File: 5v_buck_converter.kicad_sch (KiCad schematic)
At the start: 7 parts, among them U2 TPS562231DRLR

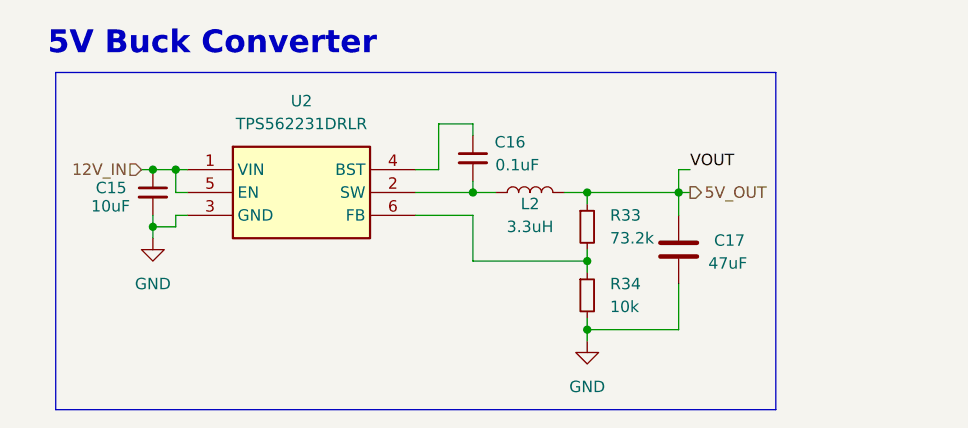
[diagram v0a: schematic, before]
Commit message: address review changes, add more output protections
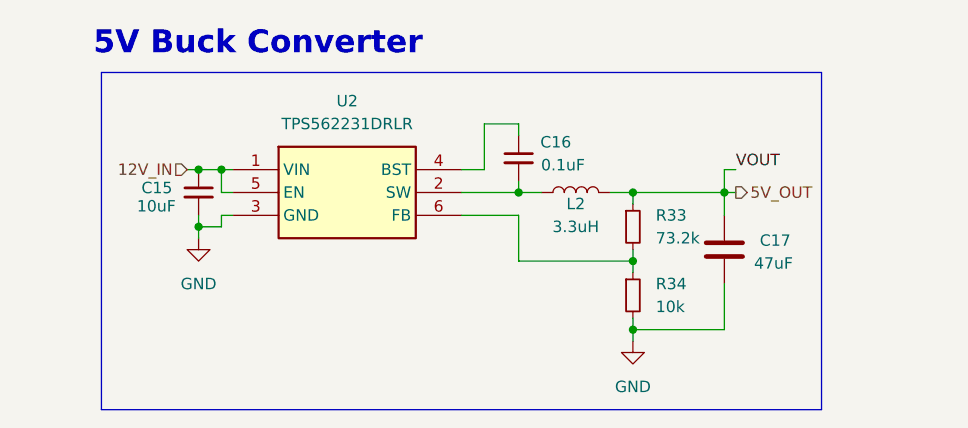
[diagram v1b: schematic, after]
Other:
- moved on the sheet: C15, C16, C17, L2, R33, R34, U2

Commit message: footprint assignment again
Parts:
- renumbered C15 to C17, C16 to C18, C17 to C19, R33 to R31, R34 to R32, U2 to U4
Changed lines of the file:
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@@
 		(on_board yes)
 		(dnp no)
-		(property "Reference" "C15"
+		(property "Reference" "C17"
 			(at 116.84 97.282 0)
 			(effects
@@
 			(project ""
 				(path "/f58400c5-df4b-4929-8d2b-33c0fe23fcd9/4f21da9f-d1d7-4b66-a00f-51f47ae1c74b"
-					(reference "C15")
+					(reference "C17")
 					(unit 1)
 				)
@@
 		(on_board yes)
 		(dnp no)
-		(property "Reference" "C17"
+		(property "Reference" "C19"
 			(at 188.976 103.124 0)
 			(effects
@@
 			(project "USBCPowerPCB"
 				(path "/f58400c5-df4b-4929-8d2b-33c0fe23fcd9/4f21da9f-d1d7-4b66-a00f-51f47ae1c74b"
-					(reference "C17")
+					(reference "C19")
 					(unit 1)
 				)
@@
 		(on_board yes)
 		(dnp no)
-		(property "Reference" "C16"
+		(property "Reference" "C18"
 			(at 164.592 92.202 0)
 			(effects
@@
 			(project "USBCPowerPCB"
 				(path "/f58400c5-df4b-4929-8d2b-33c0fe23fcd9/4f21da9f-d1d7-4b66-a00f-51f47ae1c74b"
-					(reference "C16")
+					(reference "C18")
 					(unit 1)
 				)
@@
 		(dnp no)
 		(fields_autoplaced yes)
-		(property "Reference" "R33"
+		(property "Reference" "R31"
 			(at 173.99 100.3299 0)
 			(effects
@@
 			(project "USBCPowerPCB"
 				(path "/f58400c5-df4b-4929-8d2b-33c0fe23fcd9/4f21da9f-d1d7-4b66-a00f-51f47ae1c74b"
-					(reference "R33")
+					(reference "R31")
 					(unit 1)
 				)
@@
 		(dnp no)
 		(fields_autoplaced yes)
-		(property "Reference" "R34"
+		(property "Reference" "R32"
 			(at 173.99 107.9499 0)
 			(effects
@@
 			(project ""
 				(path "/f58400c5-df4b-4929-8d2b-33c0fe23fcd9/4f21da9f-d1d7-4b66-a00f-51f47ae1c74b"
-					(reference "R34")
+					(reference "R32")
 					(unit 1)
 				)
@@
 		(dnp no)
 		(fields_autoplaced yes)
-		(property "Reference" "U2"
+		(property "Reference" "U4"
 			(at 139.7 87.63 0)
 			(effects
@@
 			(project ""
 				(path "/f58400c5-df4b-4929-8d2b-33c0fe23fcd9/4f21da9f-d1d7-4b66-a00f-51f47ae1c74b"
-					(reference "U2")
+					(reference "U4")
 					(unit 1)
 				)
@@
 		(dnp no)
 		(fields_autoplaced yes)
-		(property "Reference" "#PWR038"
+		(property "Reference" "#PWR059"
 			(at 171.45 120.65 0)
 			(effects
@@
 			(project "USBCPowerPCB"
 				(path "/f58400c5-df4b-4929-8d2b-33c0fe23fcd9/4f21da9f-d1d7-4b66-a00f-51f47ae1c74b"
-					(reference "#PWR038")
+					(reference "#PWR059")
 					(unit 1)
 				)
@@
 		(dnp no)
 		(fields_autoplaced yes)
-		(property "Reference" "#PWR037"
+		(property "Reference" "#PWR058"
 			(at 123.19 109.22 0)
 			(effects
@@
 			(project ""
 				(path "/f58400c5-df4b-4929-8d2b-33c0fe23fcd9/4f21da9f-d1d7-4b66-a00f-51f47ae1c74b"
-					(reference "#PWR037")
-					(unit 1)
-				)
+					(reference "#PWR058")
+					(unit 1)
+				)

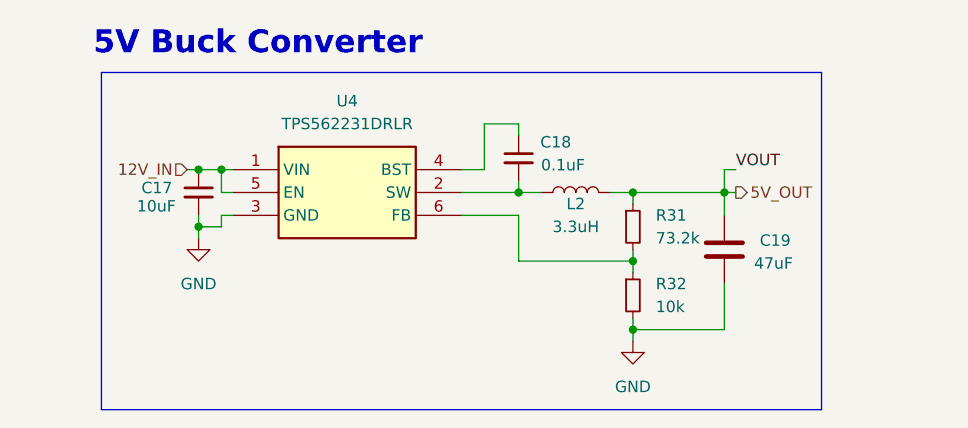
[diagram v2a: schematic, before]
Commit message: finished addressing review comments & organized bom with p/ns for everything
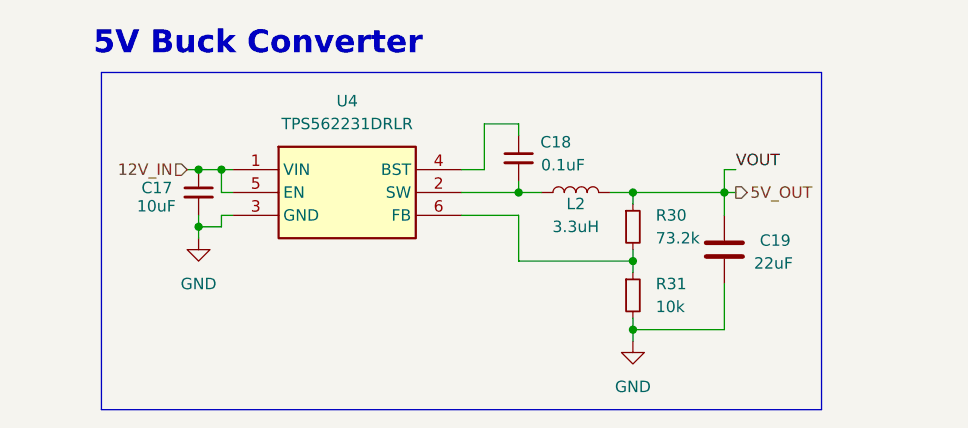
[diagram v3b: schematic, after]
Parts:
- C17: Manufacturer_Name (none) -> KEMET; Mouser Part Number (none) -> C2220C106M5RACTU; Vdc (none) -> 50V
- C18: Manufacturer_Name (none) -> KEMET; Mouser Part Number (none) -> C0805C104M5RACTU; Vdc (none) -> 50V
- C19: value 47uF -> 22uF; Manufacturer_Name (none) -> TDK; Mouser Part Number (none) -> C2012X5R1V226M125AC; Vdc (none) -> 35V
- L2: footprint Capacitor_SMD:C_1210_3225Metric -> UTSVT_Passive:INDPM110100X400N; Manufacturer_Name (none) -> Bourns; Mouser Part Number LBC3225T3R3MR -> 652-SRP1038CC-3R3M
- R30: renamed from R31; Manufacturer_Name (none) -> VISHAY; Mouser Part Number (none) -> CRCW080573K2FKEA
- R31: renamed from R32; Manufacturer_Name (none) -> VISHAY; Mouser Part Number (none) -> CRCW080510K0FKEAC
- U4: Manufacturer_Name (none) -> Texas Instruments; Mouser Part Number (none) -> 595-TPS562231DRLR
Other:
- title: (none) -> 5V Buck Converter
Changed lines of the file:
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@@
 	(paper "A4")
 	(title_block
+		(title "5V Buck Converter")
 		(company "Longhorn Racing Solar")
 		(comment 1 "https://cloud.wikis.utexas.edu/wiki/x/-qKvAQ")
@@
 		)
 		(property "Description" "Unpolarized capacitor, small symbol"
+			(at 123.19 97.79 0)
+			(effects
+				(font
+					(size 1.27 1.27)
+				)
+				(hide yes)
+			)
+		)
+		(property "Vdc" "50V"
+			(at 123.19 97.79 0)
+			(effects
+				(font
+					(size 1.27 1.27)
+				)
+				(hide yes)
+			)
+		)
+		(property "Mouser Part Number" "C2220C106M5RACTU"
+			(at 123.19 97.79 0)
+			(effects
+				(font
+					(size 1.27 1.27)
+				)
+				(hide yes)
+			)
+		)
+		(property "Manufacturer_Name" "KEMET"
 			(at 123.19 97.79 0)
 			(effects
@@
 			)
 		)
-		(property "Value" "47uF"
+		(property "Value" "22uF"
 			(at 189.23 105.664 0)
 			(effects
@@
 		)
 		(property "Description" "Unpolarized capacitor"
+			(at 181.61 104.14 0)
+			(effects
+				(font
+					(size 1.27 1.27)
+				)
+				(hide yes)
+			)
+		)
+		(property "Vdc" "35V"
+			(at 181.61 104.14 0)
+			(effects
+				(font
+					(size 1.27 1.27)
+				)
+				(hide yes)
+			)
+		)
+		(property "Manufacturer_Name" "TDK"
+			(at 181.61 104.14 0)
+			(effects
+				(font
+					(size 1.27 1.27)
+				)
+				(hide yes)
+			)
+		)
+		(property "Mouser Part Number" "C2012X5R1V226M125AC"
 			(at 181.61 104.14 0)
 			(effects
@@
 			)
 		)
+		(property "Mouser Part Number" "C0805C104M5RACTU"
+			(at 158.75 93.98 0)
+			(effects
+				(font
+					(size 1.27 1.27)
+				)
+				(hide yes)
+			)
+		)
+		(property "Vdc" "50V"
+			(at 158.75 93.98 0)
+			(effects
+				(font
+					(size 1.27 1.27)
+				)
+				(hide yes)
+			)
+		)
+		(property "Manufacturer_Name" "KEMET"
+			(at 158.75 93.98 0)
+			(effects
+				(font
+					(size 1.27 1.27)
+				)
+				(hide yes)
+			)
+		)
 		(pin "1"
 		)
@@
 		(dnp no)
 		(fields_autoplaced yes)
-		(property "Reference" "R31"
+		(property "Reference" "R30"
 			(at 173.99 100.3299 0)
 			(effects
@@
 		)
 		(property "Description" "Resistor, small symbol"
+			(at 171.45 101.6 0)
+			(effects
+				(font
+					(size 1.27 1.27)
+				)
+				(hide yes)
+			)
+		)
+		(property "Mouser Part Number" "CRCW080573K2FKEA"
+			(at 171.45 101.6 0)
+			(effects
+				(font
+					(size 1.27 1.27)
+				)
+				(hide yes)
+			)
+		)
+		(property "Vdc" ""
+			(at 171.45 101.6 0)
+			(effects
+				(font
+					(size 1.27 1.27)
+				)
+				(hide yes)
+			)
+		)
+		(property "Manufacturer_Name" "VISHAY"
 			(at 171.45 101.6 0)
 			(effects
@@
 			(project "USBCPowerPCB"
 				(path "/f58400c5-df4b-4929-8d2b-33c0fe23fcd9/4f21da9f-d1d7-4b66-a00f-51f47ae1c74b"
-					(reference "R31")
+					(reference "R30")
 					(unit 1)
 				)
@@
 		(dnp no)
 		(fields_autoplaced yes)
-		(property "Reference" "R32"
+		(property "Reference" "R31"
 			(at 173.99 107.9499 0)
 			(effects
@@
 		)
 		(property "Description" "Resistor, small symbol"
+			(at 171.45 109.22 0)
+			(effects
+				(font
+					(size 1.27 1.27)
+				)
+				(hide yes)
+			)
+		)
+		(property "Mouser Part Number" "CRCW080510K0FKEAC "
+			(at 171.45 109.22 0)
+			(effects
+				(font
+					(size 1.27 1.27)
+				)
+				(hide yes)
+			)
+		)
+		(property "Vdc" ""
+			(at 171.45 109.22 0)
+			(effects
+				(font
+					(size 1.27 1.27)
+				)
+				(hide yes)
+			)
+		)
+		(property "Manufacturer_Name" "VISHAY"
 			(at 171.45 109.22 0)
 			(effects
@@
 			(project ""
 				(path "/f58400c5-df4b-4929-8d2b-33c0fe23fcd9/4f21da9f-d1d7-4b66-a00f-51f47ae1c74b"
-					(reference "R32")
+					(reference "R31")
 					(unit 1)
 				)
@@
 			)
 		)
+		(property "Vdc" ""
+			(at 138.43 90.17 0)
+			(effects
+				(font
+					(size 1.27 1.27)
+				)
+				(hide yes)
+			)
+		)
+		(property "Manufacturer_Name" "Texas Instruments"
+			(at 138.43 90.17 0)
+			(effects
+				(font
+					(size 1.27 1.27)
+				)
+				(hide yes)
+			)
+		)
+		(property "Mouser Part Number" "595-TPS562231DRLR"
+			(at 138.43 90.17 0)
+			(effects
+				(font
+					(size 1.27 1.27)
+				)
+				(hide yes)
+			)
+		)
 		(pin "4"
 		)
@@
 		(dnp no)
 		(fields_autoplaced yes)
-		(property "Reference" "#PWR059"
+		(property "Reference" "#PWR065"
 			(at 171.45 120.65 0)
 			(effects
@@
 			(project "USBCPowerPCB"
 				(path "/f58400c5-df4b-4929-8d2b-33c0fe23fcd9/4f21da9f-d1d7-4b66-a00f-51f47ae1c74b"
-					(reference "#PWR059")
+					(reference "#PWR065")
 					(unit 1)
 				)
@@
 			)
 		)
-		(property "Footprint" "Capacitor_SMD:C_1210_3225Metric"
+		(property "Footprint" "UTSVT_Passive:INDPM110100X400N"
 			(at 165.1 97.79 0)
 			(effects
@@
 			)
 		)
-		(property "Datasheet" "https://www.mouser.com/datasheet/2/396/wound01_e-1509533.pdf"
+		(property "Datasheet" "https://www.mouser.com/datasheet/2/54/Bourns_07202023_SRP1038CC-3247812.pdf"
 			(at 165.1 97.79 0)
 			(effects
@@
 			)
 		)
-		(property "Mouser Part Number" "LBC3225T3R3MR"
+		(property "Mouser Part Number" "652-SRP1038CC-3R3M"
+			(at 165.1 97.79 0)
+			(effects
+				(font
+					(size 1.27 1.27)
+				)
+				(hide yes)
+			)
+		)
+		(property "Vdc" ""
+			(at 165.1 97.79 0)
+			(effects
+				(font
+					(size 1.27 1.27)
+				)
+				(hide yes)
+			)
+		)
+		(property "Manufacturer_Name" "Bourns"
 			(at 165.1 97.79 0)
 			(effects
@@
 		(dnp no)
 		(fields_autoplaced yes)
-		(property "Reference" "#PWR058"
+		(property "Reference" "#PWR064"
 			(at 123.19 109.22 0)
 			(effects
@@
 			(project ""
 				(path "/f58400c5-df4b-4929-8d2b-33c0fe23fcd9/4f21da9f-d1d7-4b66-a00f-51f47ae1c74b"
-					(reference "#PWR058")
+					(reference "#PWR064")
 					(unit 1)
 				)

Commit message: intermediate progress push before addressing Champers' and Lakshay's review comments
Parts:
- C18: renamed from C17; footprint Capacitor_SMD:C_0805_2012Metric -> Capacitor_SMD:C_2220_5750Metric
- renumbered C18 to C19, C19 to C20
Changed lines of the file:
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@@
 		(on_board yes)
 		(dnp no)
-		(property "Reference" "C17"
+		(property "Reference" "C18"
 			(at 116.84 97.282 0)
 			(effects
@@
 			)
 		)
-		(property "Footprint" "Capacitor_SMD:C_0805_2012Metric"
+		(property "Footprint" "Capacitor_SMD:C_2220_5750Metric"
 			(at 123.19 97.79 0)
 			(effects
@@
 			(project ""
 				(path "/f58400c5-df4b-4929-8d2b-33c0fe23fcd9/4f21da9f-d1d7-4b66-a00f-51f47ae1c74b"
-					(reference "C17")
+					(reference "C18")
 					(unit 1)
 				)
@@
 		(on_board yes)
 		(dnp no)
-		(property "Reference" "C19"
+		(property "Reference" "C20"
 			(at 188.976 103.124 0)
 			(effects
@@
 			(project "USBCPowerPCB"
 				(path "/f58400c5-df4b-4929-8d2b-33c0fe23fcd9/4f21da9f-d1d7-4b66-a00f-51f47ae1c74b"
-					(reference "C19")
+					(reference "C20")
 					(unit 1)
 				)
@@
 		(on_board yes)
 		(dnp no)
-		(property "Reference" "C18"
+		(property "Reference" "C19"
 			(at 164.592 92.202 0)
 			(effects
@@
 			(project "USBCPowerPCB"
 				(path "/f58400c5-df4b-4929-8d2b-33c0fe23fcd9/4f21da9f-d1d7-4b66-a00f-51f47ae1c74b"
-					(reference "C18")
+					(reference "C19")
 					(unit 1)
 				)
@@
 		(dnp no)
 		(fields_autoplaced yes)
-		(property "Reference" "#PWR066"
+		(property "Reference" "#PWR065"
 			(at 171.45 120.65 0)
 			(effects
@@
 			(project "USBCPowerPCB"
 				(path "/f58400c5-df4b-4929-8d2b-33c0fe23fcd9/4f21da9f-d1d7-4b66-a00f-51f47ae1c74b"
-					(reference "#PWR066")
+					(reference "#PWR065")
 					(unit 1)
 				)
@@
 		(dnp no)
 		(fields_autoplaced yes)
-		(property "Reference" "#PWR065"
+		(property "Reference" "#PWR064"
 			(at 123.19 109.22 0)
 			(effects
@@
 			(project ""
 				(path "/f58400c5-df4b-4929-8d2b-33c0fe23fcd9/4f21da9f-d1d7-4b66-a00f-51f47ae1c74b"
-					(reference "#PWR065")
-					(unit 1)
-				)
+					(reference "#PWR064")
+					(unit 1)
+				)

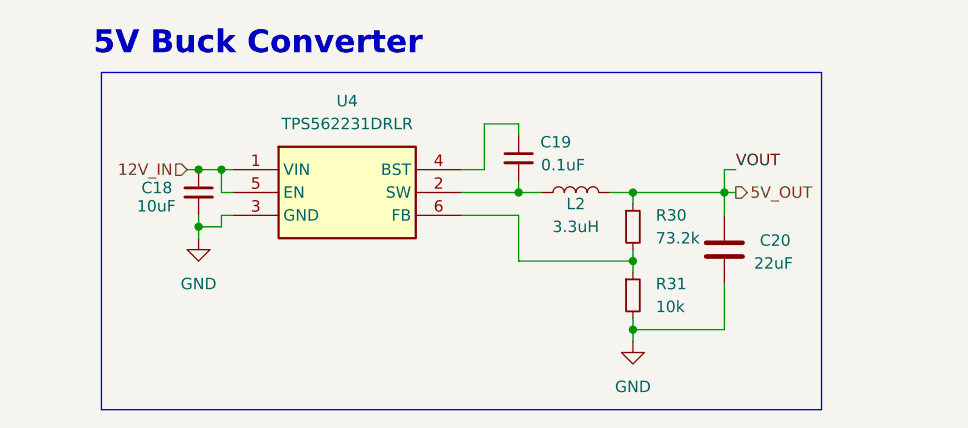
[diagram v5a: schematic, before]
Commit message: Addressed most of the review comments, fixed power protection, added bigger caps & better part selection on 12V and 5V out, changed 5V buck inductor, fixed power good & fault LEDs
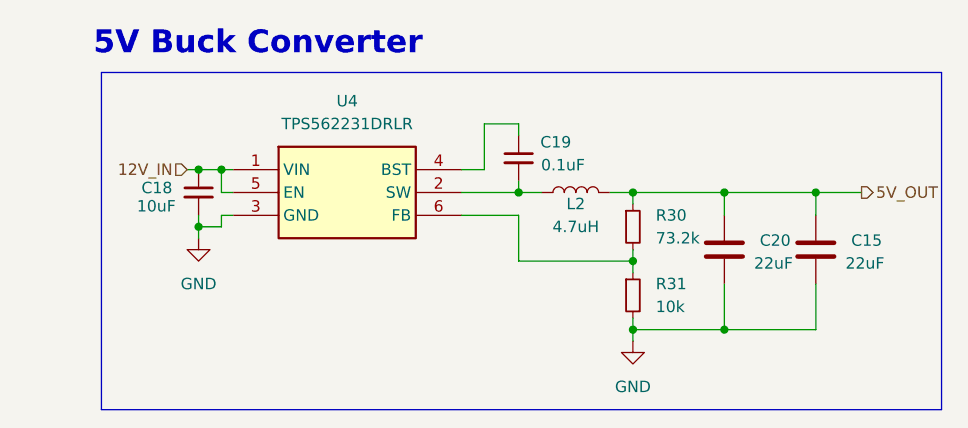
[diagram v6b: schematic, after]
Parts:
- added C15: 22uF, Capacitor_SMD:C_1210_3225Metric, symbol Device:C
- C20: footprint Capacitor_SMD:C_0805_2012Metric -> Capacitor_SMD:C_1210_3225Metric; Manufacturer_Name TDK -> Taiyo Yuden; Mouser Part Number C2012X5R1V226M125AC -> GMK325BJ226MM-P
- L2: value 3.3uH -> 4.7uH; Mouser Part Number 652-SRP1038CC-3R3M -> SRP1038CC-R47M
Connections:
- net 5V_OUT: now also C15.1
- net GND: now also C15.2

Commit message: Added ideal diode controller & mosfet for 12V buck power protection
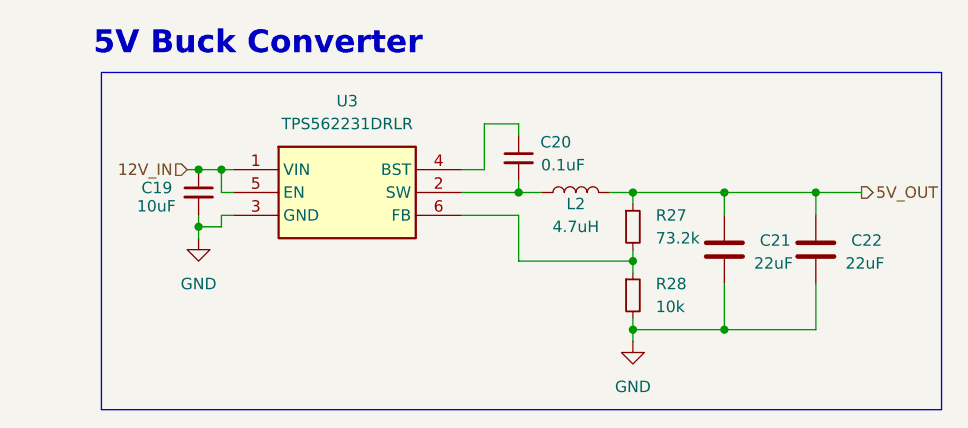
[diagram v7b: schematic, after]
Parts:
- renumbered C18 to C19, C19 to C20, C20 to C21, C15 to C22, R30 to R27, R31 to R28, U4 to U3
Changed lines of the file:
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@@
 		(on_board yes)
 		(dnp no)
-		(property "Reference" "C18"
+		(property "Reference" "C19"
 			(at 116.84 97.282 0)
 			(effects
@@
 			(project ""
 				(path "/f58400c5-df4b-4929-8d2b-33c0fe23fcd9/4f21da9f-d1d7-4b66-a00f-51f47ae1c74b"
-					(reference "C18")
+					(reference "C19")
 					(unit 1)
 				)
@@
 		(on_board yes)
 		(dnp no)
-		(property "Reference" "C20"
+		(property "Reference" "C21"
 			(at 188.976 103.124 0)
 			(effects
@@
 			(project "USBCPowerPCB"
 				(path "/f58400c5-df4b-4929-8d2b-33c0fe23fcd9/4f21da9f-d1d7-4b66-a00f-51f47ae1c74b"
-					(reference "C20")
+					(reference "C21")
 					(unit 1)
 				)
@@
 		(on_board yes)
 		(dnp no)
-		(property "Reference" "C19"
+		(property "Reference" "C20"
 			(at 164.592 92.202 0)
 			(effects
@@
 			(project "USBCPowerPCB"
 				(path "/f58400c5-df4b-4929-8d2b-33c0fe23fcd9/4f21da9f-d1d7-4b66-a00f-51f47ae1c74b"
-					(reference "C19")
+					(reference "C20")
 					(unit 1)
 				)
@@
 		(on_board yes)
 		(dnp no)
-		(property "Reference" "C15"
+		(property "Reference" "C22"
 			(at 199.136 103.124 0)
 			(effects
@@
 			(project "USBCPowerPCB"
 				(path "/f58400c5-df4b-4929-8d2b-33c0fe23fcd9/4f21da9f-d1d7-4b66-a00f-51f47ae1c74b"
-					(reference "C15")
+					(reference "C22")
 					(unit 1)
 				)
@@
 		(dnp no)
 		(fields_autoplaced yes)
-		(property "Reference" "R30"
+		(property "Reference" "R27"
 			(at 173.99 100.3299 0)
 			(effects
@@
 			(project "USBCPowerPCB"
 				(path "/f58400c5-df4b-4929-8d2b-33c0fe23fcd9/4f21da9f-d1d7-4b66-a00f-51f47ae1c74b"
-					(reference "R30")
+					(reference "R27")
 					(unit 1)
 				)
@@
 		(dnp no)
 		(fields_autoplaced yes)
-		(property "Reference" "R31"
+		(property "Reference" "R28"
 			(at 173.99 107.9499 0)
 			(effects
@@
 			(project ""
 				(path "/f58400c5-df4b-4929-8d2b-33c0fe23fcd9/4f21da9f-d1d7-4b66-a00f-51f47ae1c74b"
-					(reference "R31")
+					(reference "R28")
 					(unit 1)
 				)
@@
 		(dnp no)
 		(fields_autoplaced yes)
-		(property "Reference" "U4"
+		(property "Reference" "U3"
 			(at 139.7 87.63 0)
 			(effects
@@
 			(project ""
 				(path "/f58400c5-df4b-4929-8d2b-33c0fe23fcd9/4f21da9f-d1d7-4b66-a00f-51f47ae1c74b"
-					(reference "U4")
+					(reference "U3")
 					(unit 1)
 				)
@@
 		(dnp no)
 		(fields_autoplaced yes)
-		(property "Reference" "#PWR065"
+		(property "Reference" "#PWR062"
 			(at 171.45 120.65 0)
 			(effects
@@
 			(project "USBCPowerPCB"
 				(path "/f58400c5-df4b-4929-8d2b-33c0fe23fcd9/4f21da9f-d1d7-4b66-a00f-51f47ae1c74b"
-					(reference "#PWR065")
+					(reference "#PWR062")
 					(unit 1)
 				)
@@
 		(dnp no)
 		(fields_autoplaced yes)
-		(property "Reference" "#PWR064"
+		(property "Reference" "#PWR061"
 			(at 123.19 109.22 0)
 			(effects
@@
 			(project ""
 				(path "/f58400c5-df4b-4929-8d2b-33c0fe23fcd9/4f21da9f-d1d7-4b66-a00f-51f47ae1c74b"
-					(reference "#PWR064")
+					(reference "#PWR061")
 					(unit 1)
 				)
